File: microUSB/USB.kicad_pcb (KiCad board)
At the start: 2 copper layers, 50.2 x 31.5 mm, 36 parts, among them J1 Conn_02x12_Odd_Even, J2 Conn_02x06_Odd_Even

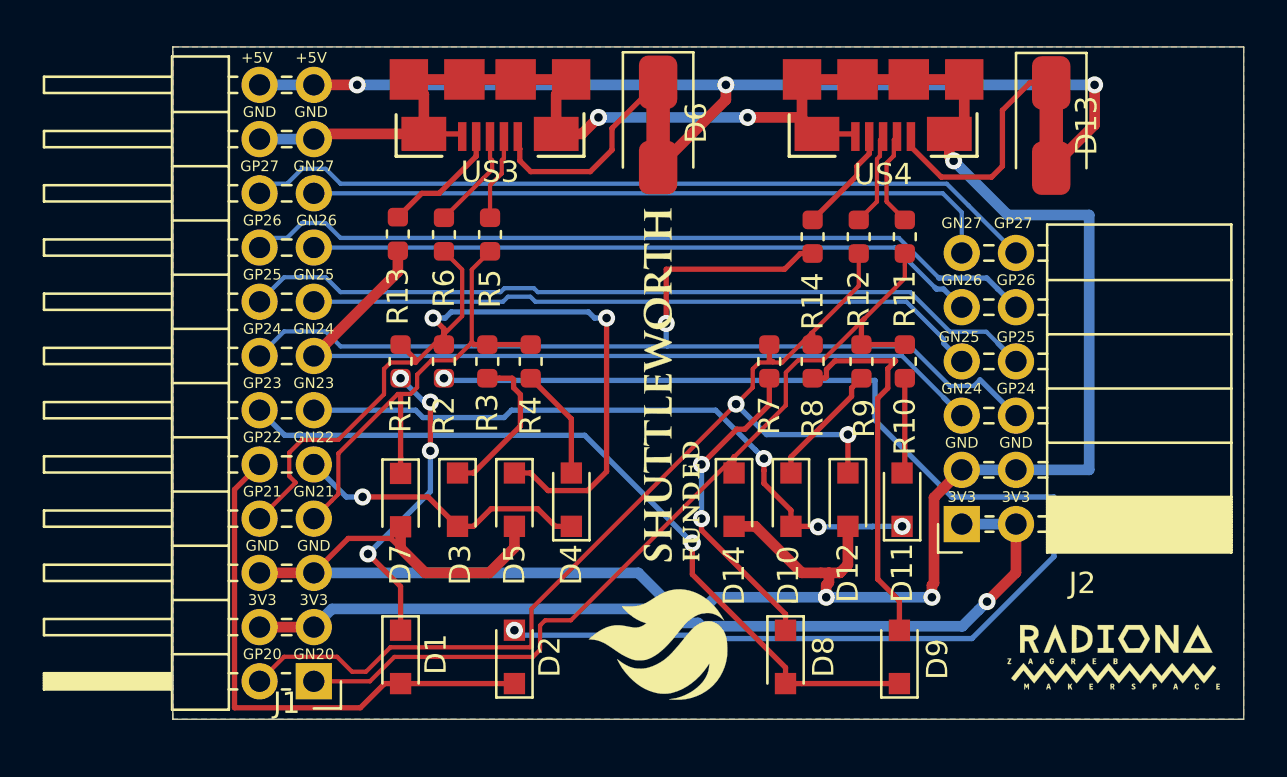
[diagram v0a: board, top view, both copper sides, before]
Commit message: Adding missing connections
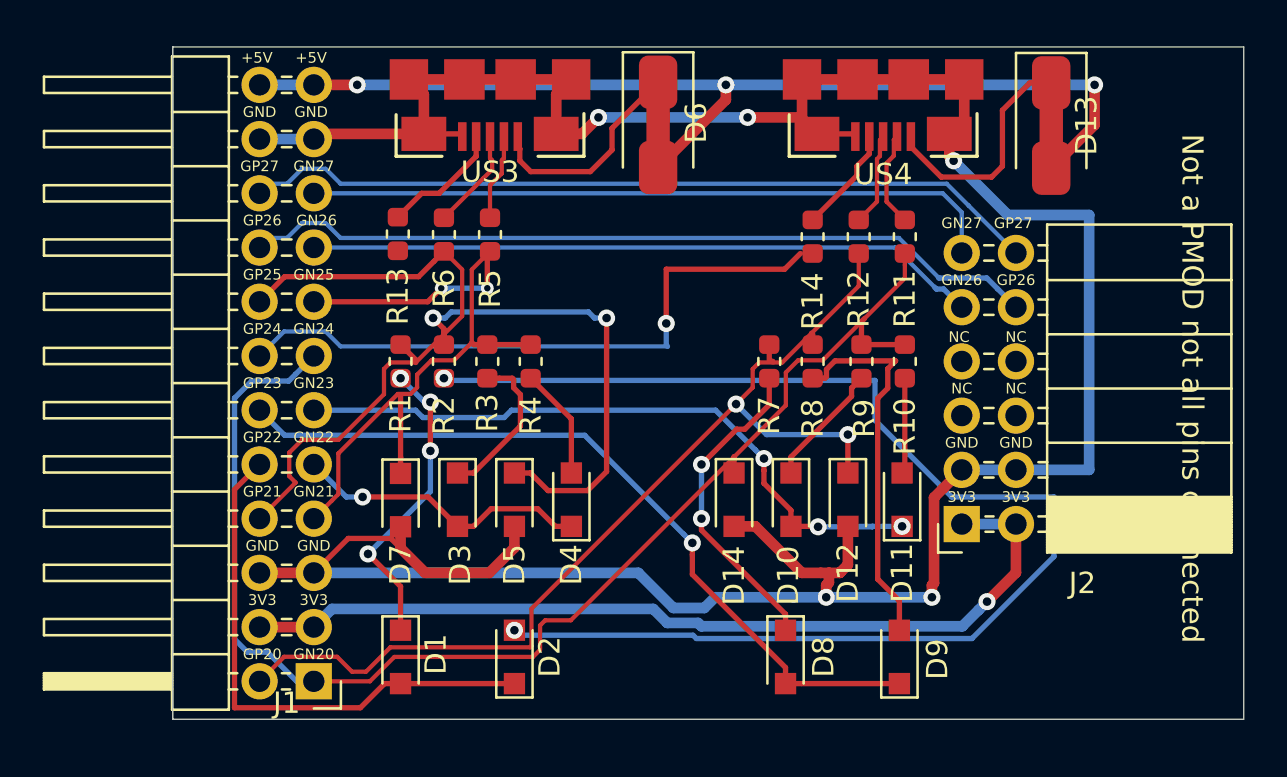
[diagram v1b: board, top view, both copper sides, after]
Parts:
- removed G*** (x2): LOGO, parts:shutleworth
- removed G***: LOGO, parts:radiona-10mm
- removed G***: LOGO, parts:radiona
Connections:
- J1 pad 13: GN24 -> USB2_FPGA_D-
- J1 pad 14: GP24 -> USB2_FPGA_D+
- J1 pad 15: GN25 -> USB1_FPGA_D-
- J1 pad 16: GP25 -> USB1_FPGA_D+
- J2 pad 5: GN24 -> (no net)
- J2 pad 6: GP24 -> (no net)
- J2 pad 7: GN25 -> (no net)
- J2 pad 8: GP25 -> (no net)
- R13 pad 1: GN24 -> (no net)
- R14 pad 1: GP24 -> (no net)
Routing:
- net GP24: track 48.6 -> 0.00 mm, vias 1 -> 0
- net GN24: track 38.1 -> 0.00 mm
- net GP25: track 37.7 -> 0.00 mm
- net GN25: track 31.8 -> 0.00 mm
- net USB2_FPGA_D+: track 48.5 -> 78.6 mm, vias 2 -> 3
- net USB2_FPGA_D-: track 42.3 -> 62.7 mm
- net USB1_FPGA_D-: track 23.4 -> 33.6 mm, vias 0 -> 2
- net USB1_FPGA_D+: track 42.5 -> 52.1 mm
- removed copper zone on B.Cu, net GND
- removed copper zone on F.Cu, net GND
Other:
- board text added: "NC"
- board text added: "Not a PMOD not all pins connected"

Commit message: Adding text not PMOD to board
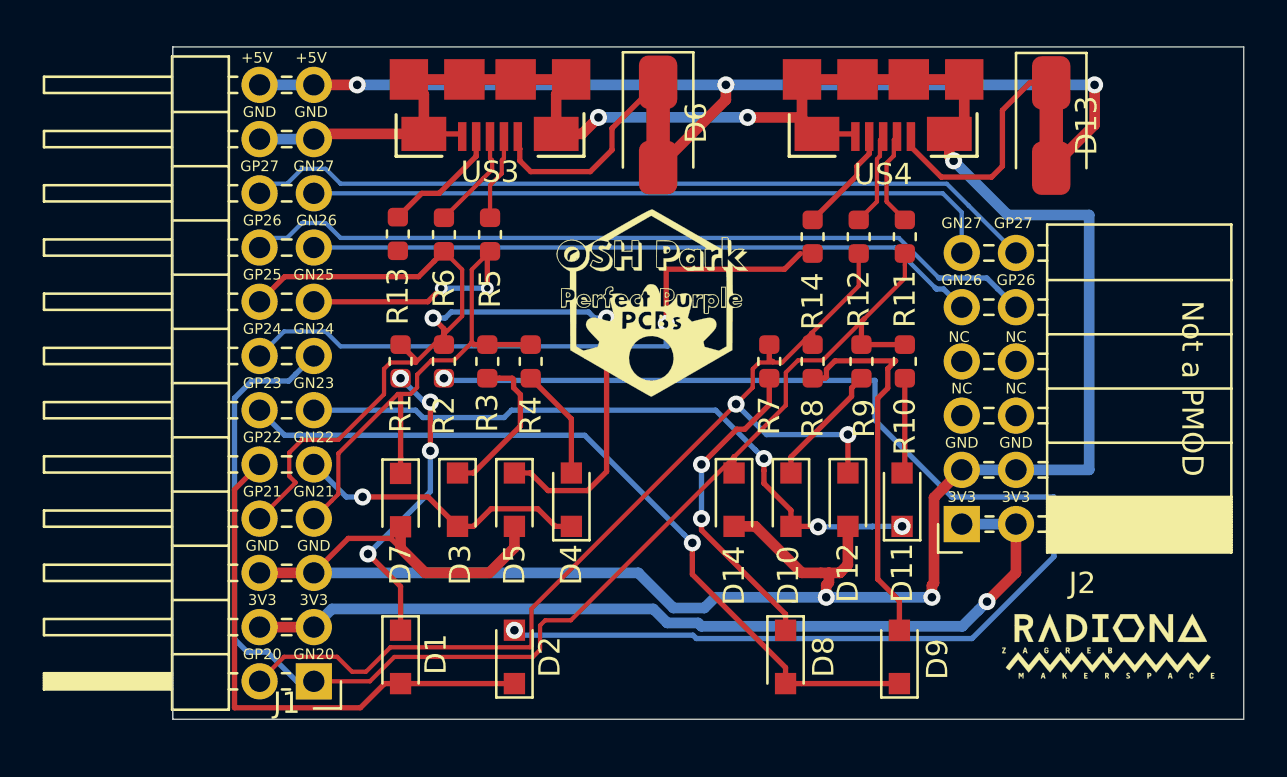
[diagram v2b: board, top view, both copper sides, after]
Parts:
- added G***: LOGO, parts:radiona-10mm, F.Cu at (163.4, 106.3)
- added G***: LOGO, parts:OSH_10x10, F.Cu at (142.1, 90.4)
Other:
- board text added: "Not a PMOD"
- board text removed: "Not a PMOD not all pins connected"
